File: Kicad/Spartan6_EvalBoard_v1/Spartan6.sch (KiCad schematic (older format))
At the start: 25 parts, among them P401 CONN_3X2, Q401 XC6SLX16, U401 24LC64T, U402 MX25L8006E, X401 XOSC

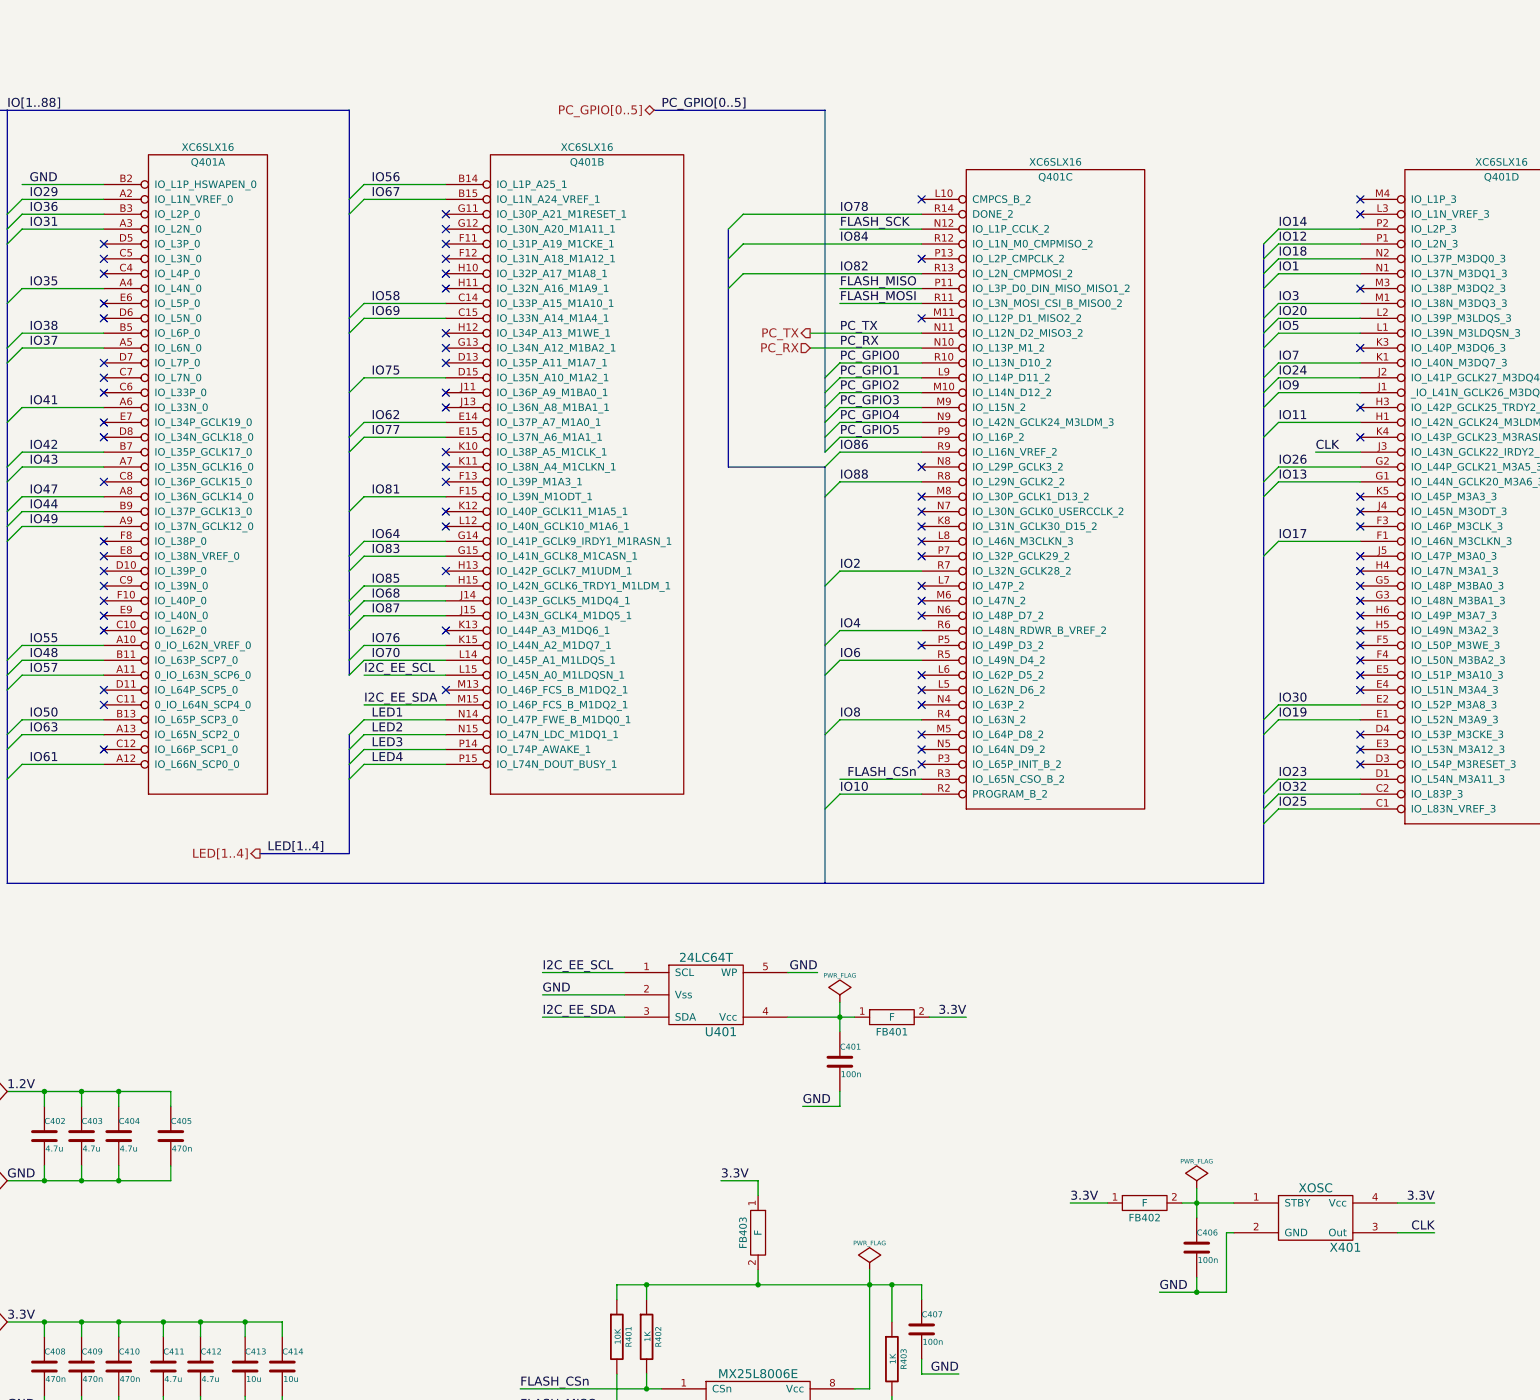
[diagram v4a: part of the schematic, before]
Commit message: Layout completed, just need to run DRC.
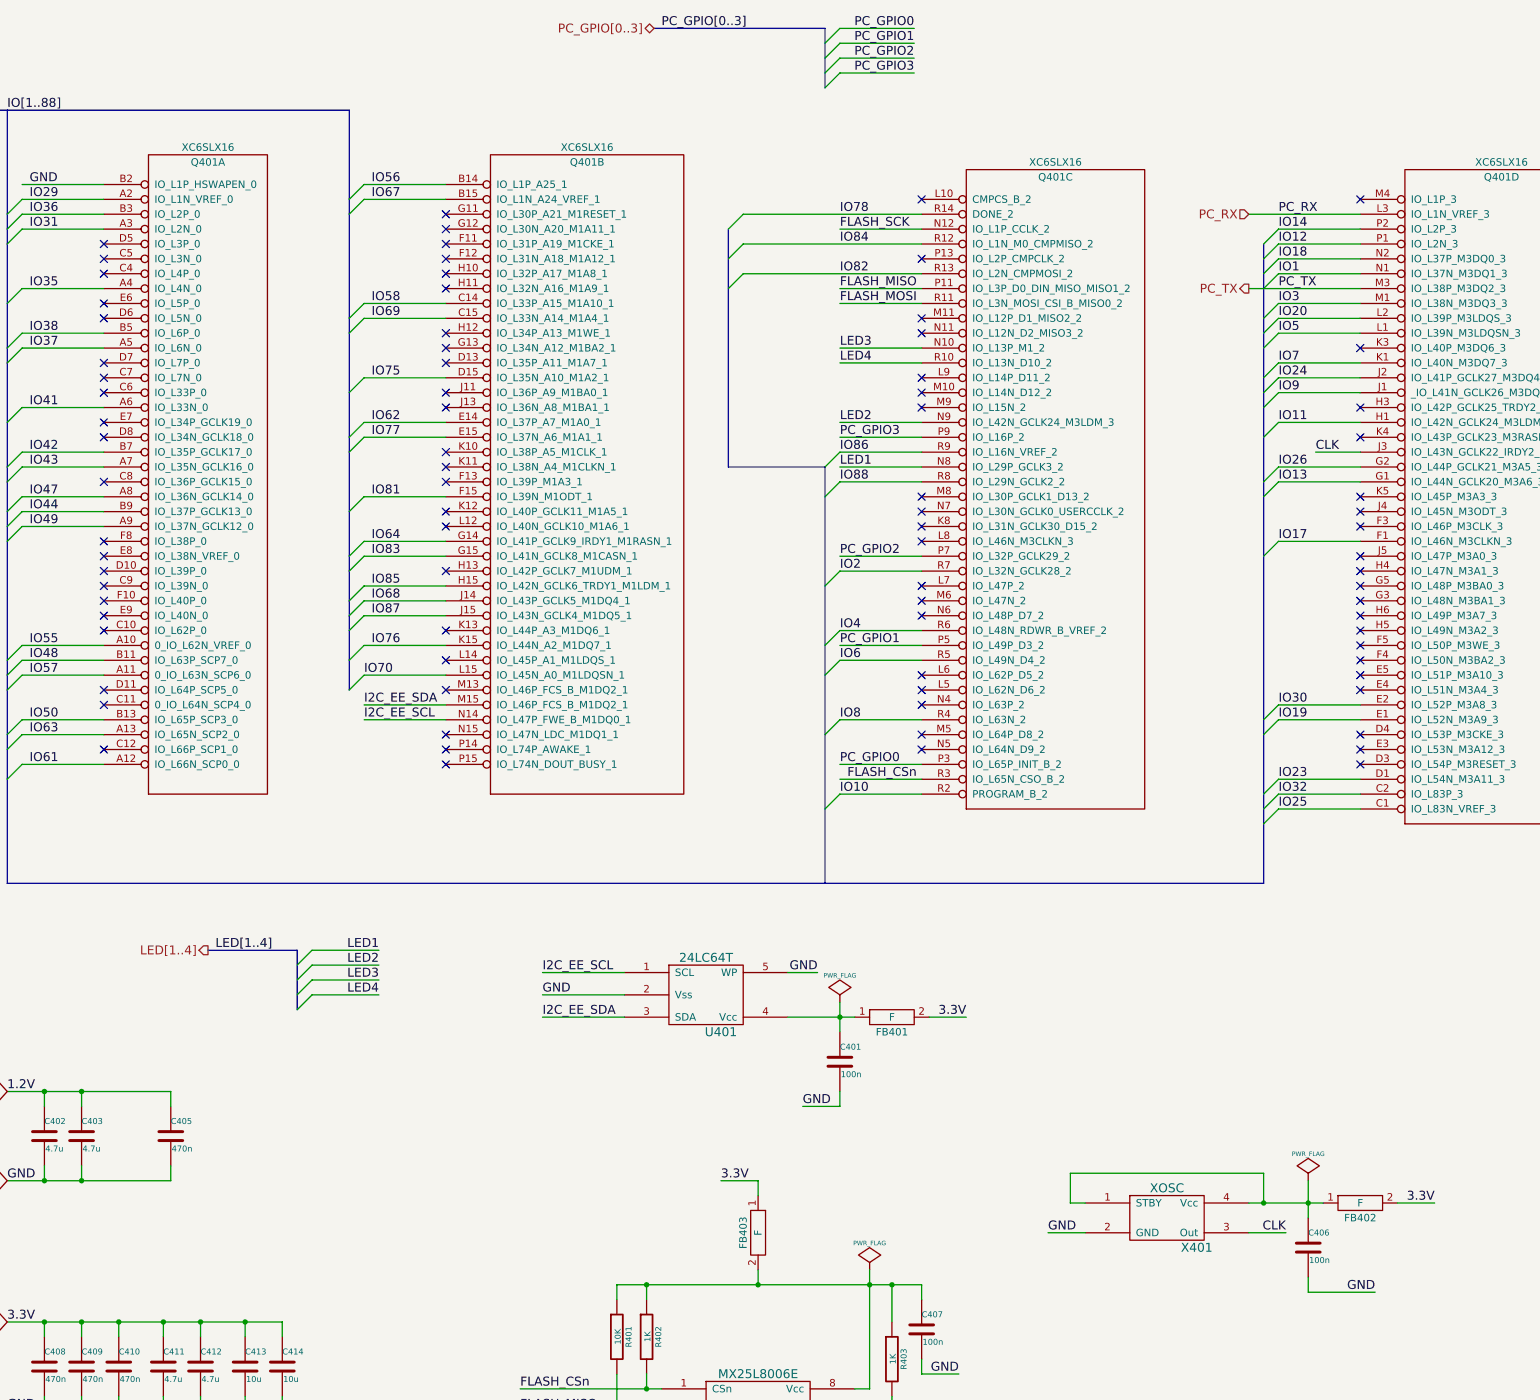
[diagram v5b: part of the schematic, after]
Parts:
- removed C404: 4.7u, Capacitors_SMD.pretty:C_0603, symbol C
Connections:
- net PC_GPIO4 is gone; now on net LED2: Q401.N9 (IO_L42N_GCLK24_M3LDM_3)
- net PC_GPIO5 is gone; now on net PC_GPIO3: Q401.P9 (IO_L16P_2)
- net 3.3V: now also FB402.2; no longer FB402.1, X401.4 (Vcc)
- net I2C_EE_SCL: now also Q401.N14 (IO_L47P_FWE_B_M1DQ0_1); no longer Q401.L15 (IO_L45N_A0_M1LDQSN_1)
- net IO70: now also Q401.L15 (IO_L45N_A0_M1LDQSN_1); no longer Q401.L14 (IO_L45P_A1_M1LDQS_1)
- net LED1: now also Q401.N8 (IO_L29P_GCLK3_2); no longer Q401.N14 (IO_L47P_FWE_B_M1DQ0_1)
- net LED2: no longer Q401.N15 (IO_L47N_LDC_M1DQ1_1)
- net LED3: now also Q401.N10 (IO_L13P_M1_2); no longer Q401.P14 (IO_L74P_AWAKE_1)
- net LED4: now also Q401.R10 (IO_L13N_D10_2); no longer Q401.P15 (IO_L74N_DOUT_BUSY_1)
- net PC_GPIO0: now also Q401.P3 (IO_L65P_INIT_B_2); no longer Q401.R10 (IO_L13N_D10_2)
- net PC_GPIO1: now also Q401.P5 (IO_L49P_D3_2); no longer Q401.L9 (IO_L14P_D11_2)
- net PC_GPIO2: now also Q401.P7 (IO_L32P_GCLK29_2); no longer Q401.M10 (IO_L14N_D12_2)
- net PC_GPIO3: no longer Q401.M9 (IO_L15N_2)
- net PC_RX: now also Q401.L3 (IO_L1N_VREF_3); no longer Q401.N10 (IO_L13P_M1_2)
- net PC_TX: now also Q401.M3 (IO_L38P_M3DQ2_3); no longer Q401.N11 (IO_L12N_D2_MISO3_2)
- net at C406.1, X401.1 (STBY): now also FB402.1, X401.4 (Vcc); no longer FB402.2
- no-connect marks 81 -> 83
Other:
- moved on the sheet: C406, FB402, X401
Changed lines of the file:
@@
-$EndComp
-$Comp
-L C C404
-U 1 1 542BA02C
-P 2100 8250
-F 0 "C404" H 2100 8350 40  0000 L CNN
-F 1 "4.7u" H 2106 8165 40  0000 L CNN
-F 2 "Capacitors_SMD.pretty:C_0603" H 2138 8100 30  0001 C CNN
-F 3 "~" H 2100 8250 60  0000 C CNN
-	1    2100 8250
-	1    0    0    -1
 $EndComp
 $Comp
@@
 L XOSC X401
 U 1 1 542B6238
-P 10150 8800
-F 0 "X401" H 10350 8600 60  0000 C CNN
-F 1 "XOSC" H 10150 9000 60  0000 C CNN
-F 2 "Eric.mod:XTAL5032" H 10100 9100 60  0001 C CNN
-F 3 "" H 10100 9100 60  0000 C CNN
-	1    10150 8800
-	1    0    0    -1
-$EndComp
-Text Label 10950 8900 2    60   ~ 0
+P 9150 8800
+F 0 "X401" H 9350 8600 60  0000 C CNN
+F 1 "XOSC" H 9150 9000 60  0000 C CNN
+F 2 "Eric.mod:XTAL5032" H 9100 9100 60  0001 C CNN
+F 3 "" H 9100 9100 60  0000 C CNN
+	1    9150 8800
+	1    0    0    -1
+$EndComp
+Text Label 9950 8900 2    60   ~ 0
 CLK
 $Comp
 L C C406
 U 1 1 542B660F
-P 9350 9000
-F 0 "C406" H 9350 9100 40  0000 L CNN
-F 1 "100n" H 9356 8915 40  0000 L CNN
-F 2 "Capacitors_SMD.pretty:C_0402" H 9388 8850 30  0001 C CNN
-F 3 "~" H 9350 9000 60  0000 C CNN
-	1    9350 9000
+P 10100 9000
+F 0 "C406" H 10100 9100 40  0000 L CNN
+F 1 "100n" H 10106 8915 40  0000 L CNN
+F 2 "Capacitors_SMD.pretty:C_0402" H 10138 8850 30  0001 C CNN
+F 3 "~" H 10100 9000 60  0000 C CNN
+	1    10100 9000
 	1    0    0    -1
 $EndComp
@@
 L F FB402
 U 1 1 542B7717
-P 9000 8700
-F 0 "FB402" H 9000 8600 50  0000 C CNN
-F 1 "F" H 9000 8700 50  0000 C CNN
-F 2 "Capacitors_SMD.pretty:C_0402" H 9000 8700 60  0001 C CNN
-F 3 "~" H 9000 8700 60  0000 C CNN
-	1    9000 8700
+P 10450 8700
+F 0 "FB402" H 10450 8600 50  0000 C CNN
+F 1 "F" H 10450 8700 50  0000 C CNN
+F 2 "Capacitors_SMD.pretty:C_0402" H 10450 8700 60  0001 C CNN
+F 3 "~" H 10450 8700 60  0000 C CNN
+	1    10450 8700
 	1    0    0    -1
 $EndComp
@@
 $EndComp
 NoConn ~ 7500 1950
-NoConn ~ 7500 2350
 NoConn ~ 7500 2750
 Entry Wire Line
@@
 Text Label 6800 7150 2    60   ~ 0
 GND
-Text Label 9100 9300 0    60   ~ 0
+Text Label 10550 9300 2    60   ~ 0
 GND
 Text Label 10950 8700 2    60   ~ 0
@@
 Text Label 13650 8650 2    60   ~ 0
 3.3V
-Text Label 3800 5450 0    60   ~ 0
-LED1
-Text Label 3800 5550 0    60   ~ 0
-LED2
-Text Label 3800 5650 0    60   ~ 0
-LED3
-Text Label 3800 5750 0    60   ~ 0
-LED4
 $Comp
 L PWR_FLAG #FLG04
@@
 L PWR_FLAG #FLG06
 U 1 1 542DC589
-P 9350 8600
-F 0 "#FLG06" H 9350 8695 30  0001 C CNN
-F 1 "PWR_FLAG" H 9350 8780 30  0000 C CNN
-F 2 "" H 9350 8600 60  0000 C CNN
-F 3 "" H 9350 8600 60  0000 C CNN
-	1    9350 8600
-	1    0    0    -1
-$EndComp
-Text Label 8500 8700 0    60   ~ 0
-3.3V
+P 10100 8550
+F 0 "#FLG06" H 10100 8645 30  0001 C CNN
+F 1 "PWR_FLAG" H 10100 8730 30  0000 C CNN
+F 2 "" H 10100 8550 60  0000 C CNN
+F 3 "" H 10100 8550 60  0000 C CNN
+	1    10100 8550
+	1    0    0    -1
+$EndComp
 Text Label 13100 3650 0    60   ~ 0
 GND
 Text Label 3750 5150 0    60   ~ 0
-I2C_EE_SCL
-Text Label 6950 2850 0    60   ~ 0
+IO70
+Text Label 9900 2550 0    60   ~ 0
 PC_TX
-Text Label 6950 2950 0    60   ~ 0
+Text Label 9900 2050 0    60   ~ 0
 PC_RX
-Text Label 6950 3050 0    60   ~ 0
-PC_GPIO0
-Text Label 6950 3150 0    60   ~ 0
-PC_GPIO1
-Text Label 6950 3250 0    60   ~ 0
-PC_GPIO2
-Text Label 6950 3350 0    60   ~ 0
+Text Label 6950 3550 0    60   ~ 0
 PC_GPIO3
-Text Label 6950 3450 0    60   ~ 0
-PC_GPIO4
-Text Label 6950 3550 0    60   ~ 0
-PC_GPIO5
-Text Label 5750 1350 0    60   ~ 0
-PC_GPIO[0..5]
-Text HLabel 5700 1350 0    60   BiDi ~ 0
-PC_GPIO[0..5]
-Entry Wire Line
-	6850 3150 6950 3050
-Entry Wire Line
-	6850 3250 6950 3150
-Entry Wire Line
-	6850 3350 6950 3250
-Entry Wire Line
-	6850 3450 6950 3350
-Entry Wire Line
-	6850 3550 6950 3450
-Entry Wire Line
-	6850 3650 6950 3550
+Text Label 5750 800  0    60   ~ 0
+PC_GPIO[0..3]
+Text HLabel 5700 800  0    60   BiDi ~ 0
+PC_GPIO[0..3]
 NoConn ~ 4300 4450
 NoConn ~ 4300 4850
 NoConn ~ 4300 4150
-Text HLabel 6750 2850 0    60   Output ~ 0
+Text HLabel 9700 2550 0    60   Output ~ 0
 PC_TX
-Text HLabel 6750 2950 0    60   Input ~ 0
+Text HLabel 9700 2050 0    60   Input ~ 0
 PC_RX
-Text Label 3100 6350 0    60   ~ 0
+Text Label 2750 7000 0    60   ~ 0
 LED[1..4]
-Text HLabel 3050 6350 0    60   Output ~ 0
+Text HLabel 2700 7000 0    60   Output ~ 0
 LED[1..4]
-Entry Wire Line
-	3650 5550 3750 5450
-Entry Wire Line
-	3650 5650 3750 5550
-Entry Wire Line
-	3650 5750 3750 5650
-Entry Wire Line
-	3650 5850 3750 5750
 $Comp
 L XC6SLX16 Q401
@@
 Wire Wire Line
 	7500 9250 7500 9350
-Connection ~ 9350 8700
-Wire Wire Line
-	9350 8600 9350 8800
-Wire Wire Line
-	9250 8700 9600 8700
-Wire Wire Line
-	9350 9200 9350 9300
 Connection ~ 6400 9250
 Wire Wire Line
@@
 	10450 3650 10150 3650
 Wire Wire Line
-	10700 8900 10950 8900
-Wire Wire Line
-	9600 8900 9550 8900
-Wire Wire Line
-	9550 8900 9550 9300
+	9700 8900 9950 8900
 Wire Wire Line
 	10700 8700 10950 8700
@@
 Wire Wire Line
 	1600 8550 1600 8450
-Connection ~ 2100 8550
 Wire Wire Line
 	1850 8550 1850 8450
@@
 	1350 7950 2450 7950
 Wire Wire Line
-	2100 7950 2100 8050
-Wire Wire Line
 	1850 7950 1850 8050
-Connection ~ 2100 7950
 Connection ~ 1850 7950
-Wire Wire Line
-	2100 8450 2100 8550
 Connection ~ 1600 7950
 Connection ~ 1600 8550
@@
 	7550 7450 7800 7450
 Wire Wire Line
-	9550 9300 9100 9300
-Connection ~ 9350 9300
-Wire Wire Line
-	3750 5550 4300 5550
-Wire Wire Line
-	4300 5650 3750 5650
-Wire Wire Line
-	4300 5750 3750 5750
-Wire Wire Line
-	4300 5450 3750 5450
-Wire Wire Line
-	8750 8700 8500 8700
+	10550 9300 10100 9300
 Wire Wire Line
 	13450 3850 13350 3850
@@
 	4300 5150 3750 5150
 Wire Wire Line
-	6750 2850 7500 2850
-Wire Wire Line
-	6750 2950 7500 2950
-Wire Wire Line
-	7500 3050 6950 3050
-Wire Wire Line
-	7500 3150 6950 3150
-Wire Wire Line
-	7500 3250 6950 3250
-Wire Wire Line
-	7500 3350 6950 3350
-Wire Wire Line
-	7500 3450 6950 3450
+	9700 2550 10450 2550
+Wire Wire Line
+	9700 2050 10450 2050
 Wire Wire Line
 	7500 3550 6950 3550
 Wire Bus Line
-	5700 1350 6850 1350
+	5700 800  6850 800
 Wire Bus Line
-	3650 1350 3650 5150
+	3650 1350 3650 5250
 Wire Bus Line
-	3650 5550 3650 6350
-Wire Bus Line
-	3650 6350 3050 6350
+	3300 7000 2700 7000
 $Comp
 L XC6SLX16 Q401
@@
 Wire Wire Line
 	4300 4550 3750 4550
-NoConn ~ 4300 5250
 Text Label 3750 5350 0    60   ~ 0
 I2C_EE_SDA
@@
 Text Label 6950 2450 0    60   ~ 0
 IO82
-NoConn ~ 7500 3750
 NoConn ~ 7500 3950
 NoConn ~ 7500 4050
 NoConn ~ 7500 4150
 NoConn ~ 7500 4250
-NoConn ~ 7500 4350
 NoConn ~ 7500 4550
 NoConn ~ 7500 4650
 NoConn ~ 7500 4750
-NoConn ~ 7500 4950
 NoConn ~ 7500 5150
 NoConn ~ 7500 5250
@@
 NoConn ~ 7500 5550
 NoConn ~ 7500 5650
-NoConn ~ 7500 5750
 NoConn ~ 10450 1950
-NoConn ~ 10450 2050
-NoConn ~ 10450 2550
 NoConn ~ 10450 2950
 NoConn ~ 10450 3350
@@
 NoConn ~ 10450 5650
 NoConn ~ 10450 5750
-Wire Bus Line
-	6850 1350 6850 3650
 Entry Wire Line
 	6200 2150 6300 2050
@@
 IO84
 Wire Wire Line
-	7500 2250 6300 2250
-Wire Wire Line
 	10450 2250 9900 2250
 Entry Wire Line
@@
 	4300 1850 3750 1850
 Wire Wire Line
-	4300 5050 3750 5050
-Entry Wire Line
-	3650 5150 3750 5050
-Wire Wire Line
 	4300 4650 3750 4650
 Entry Wire Line
@@
 Wire Wire Line
 	4300 2650 3750 2650
-Text Label 3800 5050 0    60   ~ 0
-IO70
 Text Label 3800 4650 0    60   ~ 0
 IO68
@@
 Text Label 9900 2150 0    60   ~ 0
 IO14
+Wire Wire Line
+	9700 8700 10200 8700
+Wire Wire Line
+	10100 9300 10100 9200
+Text Label 8350 8900 0    60   ~ 0
+GND
+Wire Wire Line
+	8600 8900 8350 8900
+Wire Wire Line
+	10100 8550 10100 8800
+Connection ~ 10100 8700
+Wire Wire Line
+	8600 8700 8500 8700
+Wire Wire Line
+	8500 8700 8500 8500
+Wire Wire Line
+	8500 8500 9800 8500
+Wire Wire Line
+	9800 8500 9800 8700
+Connection ~ 9800 8700
+NoConn ~ 7500 3350
+NoConn ~ 7500 3250
+NoConn ~ 7500 3150
+Wire Wire Line
+	7500 2250 6300 2250
+Wire Bus Line
+	6850 800  6850 1200
+Entry Wire Line
+	6850 900  6950 800
+Entry Wire Line
+	6850 1000 6950 900
+Entry Wire Line
+	6850 1100 6950 1000
+Entry Wire Line
+	6850 1200 6950 1100
+Wire Wire Line
+	6950 1100 7450 1100
+Wire Wire Line
+	6950 1000 7450 1000
+Wire Wire Line
+	6950 900  7450 900
+Wire Wire Line
+	6950 800  7450 800
+Text Label 7450 800  2    60   ~ 0
+PC_GPIO0
+Text Label 7450 900  2    60   ~ 0
+PC_GPIO1
+Text Label 7450 1000 2    60   ~ 0
+PC_GPIO2
+Text Label 7450 1100 2    60   ~ 0
+PC_GPIO3
+Wire Wire Line
+	7500 4350 6950 4350
+Text Label 6950 4350 0    60   ~ 0
+PC_GPIO2
+Wire Wire Line
+	7500 5750 6950 5750
+Wire Wire Line
+	7500 4950 6950 4950
+Text Label 6950 4950 0    60   ~ 0
+PC_GPIO1
+Text Label 6950 5750 0    60   ~ 0
+PC_GPIO0
+Wire Bus Line
+	3300 7000 3300 7400
+Entry Wire Line
+	3300 7100 3400 7000
+Entry Wire Line
+	3300 7200 3400 7100
+Entry Wire Line
+	3300 7300 3400 7200
+Entry Wire Line
+	3300 7400 3400 7300
+Wire Wire Line
+	3400 7000 3850 7000
+Wire Wire Line
+	3400 7100 3850 7100
+Wire Wire Line
+	3400 7200 3850 7200
+Wire Wire Line
+	3400 7300 3850 7300
+Text Label 3850 7300 2    60   ~ 0
+LED4
+Text Label 3850 7200 2    60   ~ 0
+LED3
+Text Label 3850 7100 2    60   ~ 0
+LED2
+Text Label 3850 7000 2    60   ~ 0
+LED1
+NoConn ~ 4300 5550
+NoConn ~ 4300 5750
+NoConn ~ 4300 5250
+Wire Wire Line
+	7500 3750 6950 3750
+Wire Wire Line
+	7500 3450 6950 3450
+Wire Wire Line
+	7500 2950 6950 2950
+Text Label 6950 3750 0    60   ~ 0
+LED1
+Text Label 6950 3450 0    60   ~ 0
+LED2
+Text Label 6950 2950 0    60   ~ 0
+LED3
+NoConn ~ 7500 2850
+Wire Wire Line
+	7500 3050 6950 3050
+Text Label 6950 3050 0    60   ~ 0
+LED4
+NoConn ~ 7500 2350
+NoConn ~ 4300 5650
+Entry Wire Line
+	3650 5250 3750 5150
+NoConn ~ 4300 5050
+Wire Wire Line
+	4300 5450 3750 5450
+Text Label 3750 5450 0    60   ~ 0
+I2C_EE_SCL
 $EndSCHEMATC
